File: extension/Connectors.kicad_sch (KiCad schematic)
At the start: 2 parts, among them X701 MB2, X702 MB1

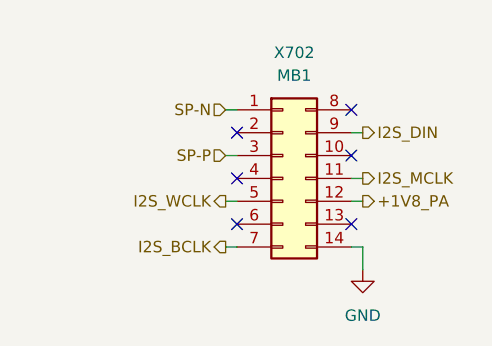
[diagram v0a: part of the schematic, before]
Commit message: Reduce radius to 8.4 mm
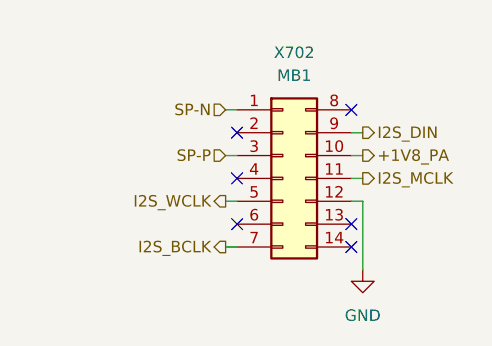
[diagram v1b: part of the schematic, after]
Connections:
- net +1V8_PA: now also X702.10 (Pin_10); no longer X702.12 (Pin_12)
- net GND: now also X702.12 (Pin_12); no longer X702.14 (Pin_14)
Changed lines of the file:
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@@
+	)
+	(no_connect
+		(at 208.28 104.14)
 	)
 	(no_connect
@@
 		(at 102.87 99.06)
 	)
-	(no_connect
-		(at 208.28 93.98)
-	)
 	(wire
 		(pts
@@
 	(wire
 		(pts
-			(xy 208.28 104.14) (xy 209.55 104.14)
-		)
-		(stroke
-			(width 0)
-			(type default)
-		)
-	)
-	(wire
-		(pts
 			(xy 102.87 88.9) (xy 99.06 88.9)
 		)
@@
 	(wire
 		(pts
-			(xy 209.55 104.14) (xy 209.55 106.68)
+			(xy 209.55 99.06) (xy 209.55 106.68)
 		)
 		(stroke
@@
 	(wire
 		(pts
+			(xy 208.28 93.98) (xy 209.55 93.98)
+		)
+		(stroke
+			(width 0)
+			(type default)
+		)
+	)
+	(wire
+		(pts
+			(xy 102.87 91.44) (xy 95.25 91.44)
+		)
+		(stroke
+			(width 0)
+			(type default)
+		)
+	)
+	(wire
+		(pts
+			(xy 194.31 104.14) (xy 195.58 104.14)
+		)
+		(stroke
+			(width 0)
+			(type default)
+		)
+	)
+	(wire
+		(pts
+			(xy 102.87 78.74) (xy 102.87 80.01)
+		)
+		(stroke
+			(width 0)
+			(type default)
+		)
+	)
+	(wire
+		(pts
+			(xy 208.28 96.52) (xy 209.55 96.52)
+		)
+		(stroke
+			(width 0)
+			(type default)
+		)
+	)
+	(wire
+		(pts
 			(xy 208.28 99.06) (xy 209.55 99.06)
-		)
-		(stroke
-			(width 0)
-			(type default)
-		)
-	)
-	(wire
-		(pts
-			(xy 102.87 91.44) (xy 95.25 91.44)
-		)
-		(stroke
-			(width 0)
-			(type default)
-		)
-	)
-	(wire
-		(pts
-			(xy 194.31 104.14) (xy 195.58 104.14)
-		)
-		(stroke
-			(width 0)
-			(type default)
-		)
-	)
-	(wire
-		(pts
-			(xy 102.87 78.74) (xy 102.87 80.01)
-		)
-		(stroke
-			(width 0)
-			(type default)
-		)
-	)
-	(wire
-		(pts
-			(xy 208.28 96.52) (xy 209.55 96.52)
 		)
 		(stroke
@@
 	(hierarchical_label "+1V8_PA"
 		(shape output)
-		(at 209.55 99.06 0)
-		(effects
-			(font
+		(at 209.55 93.98 0)
+		(effects
+			(font
